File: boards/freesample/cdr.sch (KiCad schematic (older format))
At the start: 66 parts, among them J6 XILINX_JTAG, U13 SIP32408, U5 TLK10232, U6 LMK61PD0A2

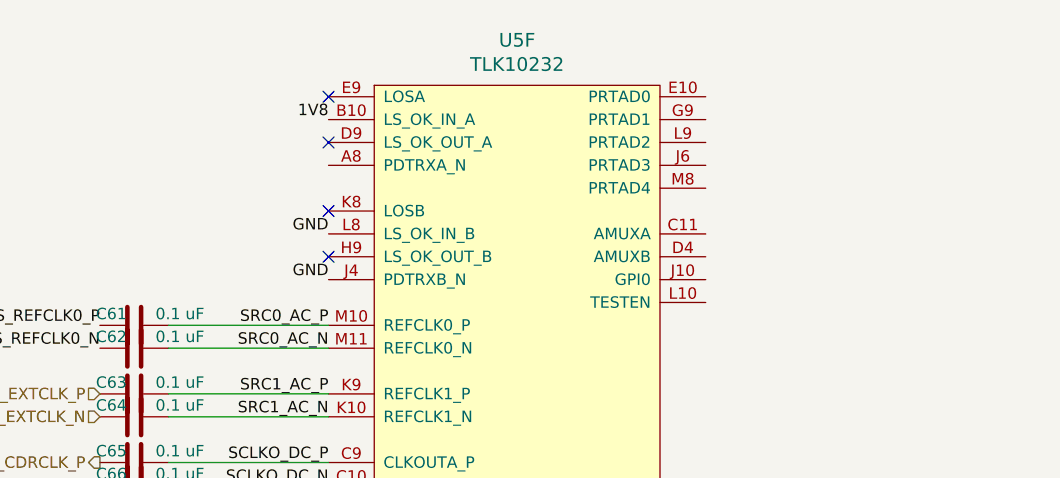
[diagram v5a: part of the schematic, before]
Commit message: Continued schematic capture work. Hooked up most SoM connectors.
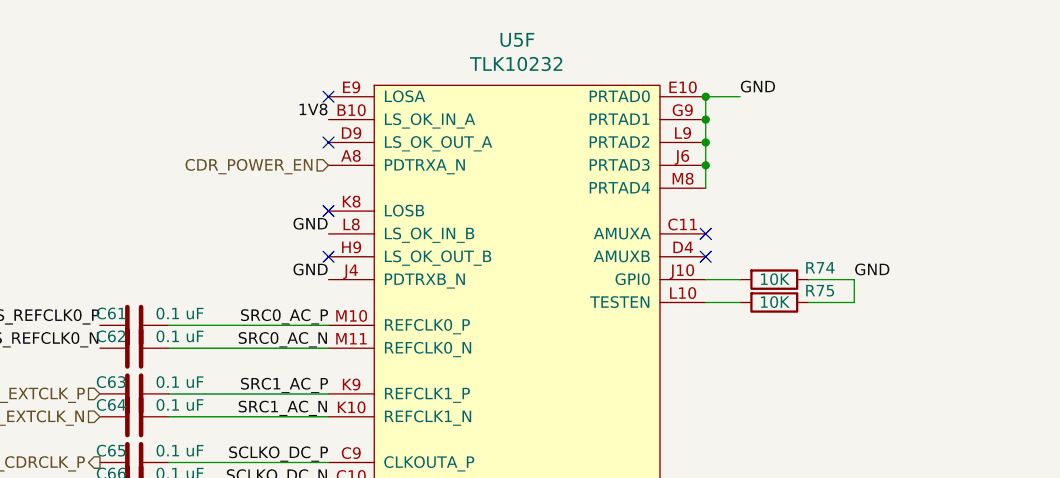
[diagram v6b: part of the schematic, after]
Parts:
- added R74, R75: 10K, symbol device:R
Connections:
- net GND: now also U5.E10 (PRTAD0), U5.G9 (PRTAD1), U5.J6 (PRTAD3), U5.L9 (PRTAD2), U5.M8 (PRTAD4), R74.1, R75.1
- net CDR_POWER_EN: now reaches U5.A8 (PDTRXA_N)
- net at U5.J10 (GPI0): now also R74.2
- net at U5.L10 (TESTEN): now also R75.2
- no-connect marks 29 -> 31
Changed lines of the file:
@@
 Sheet 4 12
 Title "FREESAMPLE Oscilloscope"
-Date "2019-02-26"
+Date "2019-03-10"
 Rev "0.1"
 Comp "Andrew D. Zonenberg / Antikernel Labs"
 Comment1 "CDR SERDES"
-Comment2 ""
+Comment2 "Ready for review"
 Comment3 ""
 Comment4 ""
@@
 Text Notes 550  11150 0    100  ~ 0
 CDR PLL reference clock
+Text HLabel 5300 1150 0    50   Input ~ 0
+CDR_POWER_EN
+NoConn ~ 6950 1550
+$Comp
+L device:R R74
+U 1 1 5D4BF0FF
+P 7250 1650
+F 0 "R74" V 7200 1850 50  0000 C CNN
+F 1 "10K" V 7250 1650 50  0000 C CNN
+F 2 "" V 7180 1650 50  0001 C CNN
+F 3 "" H 7250 1650 50  0001 C CNN
+	1    7250 1650
+	0    1    1    0
+$EndComp
+Text Label 7600 1650 0    50   ~ 0
+GND
+Wire Wire Line
+	7600 1650 7400 1650
+Wire Wire Line
+	7100 1650 6950 1650
+$Comp
+L device:R R75
+U 1 1 5D4D8BAB
+P 7250 1750
+F 0 "R75" V 7200 1950 50  0000 C CNN
+F 1 "10K" V 7250 1750 50  0000 C CNN
+F 2 "" V 7180 1750 50  0001 C CNN
+F 3 "" H 7250 1750 50  0001 C CNN
+	1    7250 1750
+	0    1    1    0
+$EndComp
+Wire Wire Line
+	7100 1750 6950 1750
+Wire Wire Line
+	7600 1650 7600 1750
+Wire Wire Line
+	7600 1750 7400 1750
+Wire Wire Line
+	6950 1250 6950 1150
+Connection ~ 6950 950
+Wire Wire Line
+	6950 950  6950 850
+Connection ~ 6950 1050
+Wire Wire Line
+	6950 1050 6950 950
+Connection ~ 6950 1150
+Wire Wire Line
+	6950 1150 6950 1050
+Text Label 7100 850  0    50   ~ 0
+GND
+Connection ~ 6950 850
+Wire Wire Line
+	6950 850  7100 850
+NoConn ~ 6950 1450
 $EndSCHEMATC

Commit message: Specified part number for AC coupling caps
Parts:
- C56, C57, C61, C62, C63, C64, C65, C66: value 0.1 uF -> 530Z104KT10T
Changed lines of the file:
@@
 Sheet 4 12
 Title "FREESAMPLE Oscilloscope"
-Date "2019-03-11"
+Date "2019-03-13"
 Rev "0.1"
 Comp "Andrew D. Zonenberg / Antikernel Labs"
@@
 P 1200 1100
 F 0 "C56" V 1150 1000 50  0000 C CNN
-F 1 "0.1 uF" V 1150 1300 50  0000 C CNN
+F 1 "530Z104KT10T" V 950 1300 50  0000 C CNN
 F 2 "" H 1238 950 50  0001 C CNN
 F 3 "" H 1200 1100 50  0001 C CNN
@@
 P 1200 1300
 F 0 "C57" V 1150 1200 50  0000 C CNN
-F 1 "0.1 uF" V 1150 1500 50  0000 C CNN
+F 1 "530Z104KT10T" V 850 1500 50  0000 C CNN
 F 2 "" H 1238 1150 50  0001 C CNN
 F 3 "" H 1200 1300 50  0001 C CNN
@@
 P 4450 1850
 F 0 "C61" V 4400 1750 50  0000 C CNN
-F 1 "0.1 uF" V 4400 2050 50  0000 C CNN
+F 1 "530Z104KT10T" V 4200 2050 50  0000 C CNN
 F 2 "" H 4488 1700 50  0001 C CNN
 F 3 "" H 4450 1850 50  0001 C CNN
@@
 P 4450 1950
 F 0 "C62" V 4400 1850 50  0000 C CNN
-F 1 "0.1 uF" V 4400 2150 50  0000 C CNN
+F 1 "530Z104KT10T" V 4200 2150 50  0000 C CNN
 F 2 "" H 4488 1800 50  0001 C CNN
 F 3 "" H 4450 1950 50  0001 C CNN
@@
 P 4450 2150
 F 0 "C63" V 4400 2050 50  0000 C CNN
-F 1 "0.1 uF" V 4400 2350 50  0000 C CNN
+F 1 "530Z104KT10T" V 5000 2350 50  0000 C CNN
 F 2 "" H 4488 2000 50  0001 C CNN
 F 3 "" H 4450 2150 50  0001 C CNN
@@
 P 4450 2250
 F 0 "C64" V 4400 2150 50  0000 C CNN
-F 1 "0.1 uF" V 4400 2450 50  0000 C CNN
+F 1 "530Z104KT10T" V 5000 2450 50  0000 C CNN
 F 2 "" H 4488 2100 50  0001 C CNN
 F 3 "" H 4450 2250 50  0001 C CNN
@@
 P 4450 2450
 F 0 "C65" V 4400 2350 50  0000 C CNN
-F 1 "0.1 uF" V 4400 2650 50  0000 C CNN
+F 1 "530Z104KT10T" V 4900 2650 50  0000 C CNN
 F 2 "" H 4488 2300 50  0001 C CNN
 F 3 "" H 4450 2450 50  0001 C CNN
@@
 P 4450 2550
 F 0 "C66" V 4400 2450 50  0000 C CNN
-F 1 "0.1 uF" V 4400 2750 50  0000 C CNN
+F 1 "530Z104KT10T" V 4900 2750 50  0000 C CNN
 F 2 "" H 4488 2400 50  0001 C CNN
 F 3 "" H 4450 2550 50  0001 C CNN
